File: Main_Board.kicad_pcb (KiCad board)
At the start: 2 copper layers, 90 x 90 mm, 61 parts, among them J1 DAC_12-bits, J2 Measurement_Header, Q1 Q_PNP_BCE, Q2 Q_NPN_BCE, U1 AD667, U2 LF356

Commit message: Stuff
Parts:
- added U3: AD558JN, Package_DIP:DIP-16_W7.62mm_Socket, F.Cu at (81.0, 85.0)
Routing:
- net /Vin: track 173.3 -> 148.1 mm
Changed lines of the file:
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@@
     (thickness 1.6)
     (drawings 11)
-    (tracks 396)
+    (tracks 398)
     (zones 0)
-    (modules 61)
-    (nets 57)
+    (modules 62)
+    (nets 73)
   )
   (page A4)
   (layers
     (0 F.Cu signal)
-    (31 B.Cu signal hide)
+    (31 B.Cu signal)
     (32 B.Adhes user)
     (33 F.Adhes user)
@@
   (net 55 "Net-(+15V1-Pad3)")
   (net 56 "Net-(+15V1-Pad2)")
+  (net 57 "Net-(U3-Pad16)")
+  (net 58 "Net-(U3-Pad8)")
+  (net 59 "Net-(U3-Pad15)")
+  (net 60 "Net-(U3-Pad7)")
+  (net 61 "Net-(U3-Pad14)")
+  (net 62 "Net-(U3-Pad6)")
+  (net 63 "Net-(U3-Pad13)")
+  (net 64 "Net-(U3-Pad5)")
+  (net 65 "Net-(U3-Pad12)")
+  (net 66 "Net-(U3-Pad4)")
+  (net 67 "Net-(U3-Pad11)")
+  (net 68 "Net-(U3-Pad3)")
+  (net 69 "Net-(U3-Pad10)")
+  (net 70 "Net-(U3-Pad2)")
+  (net 71 "Net-(U3-Pad9)")
+  (net 72 "Net-(U3-Pad1)")
   (net_class Default "This is the default net class."
     (clearance 0.2)
@@
     (add_net "Net-(U2-Pad5)")
     (add_net "Net-(U2-Pad8)")
+    (add_net "Net-(U3-Pad1)")
+    (add_net "Net-(U3-Pad10)")
+    (add_net "Net-(U3-Pad11)")
+    (add_net "Net-(U3-Pad12)")
+    (add_net "Net-(U3-Pad13)")
+    (add_net "Net-(U3-Pad14)")
+    (add_net "Net-(U3-Pad15)")
+    (add_net "Net-(U3-Pad16)")
+    (add_net "Net-(U3-Pad2)")
+    (add_net "Net-(U3-Pad3)")
+    (add_net "Net-(U3-Pad4)")
+    (add_net "Net-(U3-Pad5)")
+    (add_net "Net-(U3-Pad6)")
+    (add_net "Net-(U3-Pad7)")
+    (add_net "Net-(U3-Pad8)")
+    (add_net "Net-(U3-Pad9)")
+  )
+  (module Package_DIP:DIP-16_W7.62mm_Socket (layer F.Cu)
+    (at 81 85)
+    (descr "16-lead though-hole mounted DIP package, row spacing 7.62 mm (300 mils), Socket")
+    (tags "THT DIP DIL PDIP 2.54mm 7.62mm 300mil Socket")
+    (fp_text reference U3 (at 3.81 -2.33) (layer F.SilkS)
+      (effects (font (size 1 1) (thickness 0.15)))
+    )
+    (fp_text value AD558JN (at 3.81 20.11) (layer F.Fab)
+      (effects (font (size 1 1) (thickness 0.15)))
+    )
+    (fp_text user %R (at 3.81 8.89) (layer F.Fab)
+      (effects (font (size 1 1) (thickness 0.15)))
+    )
+    (fp_line (start 9.15 -1.6) (end -1.55 -1.6) (layer F.CrtYd) (width 0.05))
+    (fp_line (start 9.15 19.4) (end 9.15 -1.6) (layer F.CrtYd) (width 0.05))
+    (fp_line (start -1.55 19.4) (end 9.15 19.4) (layer F.CrtYd) (width 0.05))
+    (fp_line (start -1.55 -1.6) (end -1.55 19.4) (layer F.CrtYd) (width 0.05))
+    (fp_line (start 8.95 -1.39) (end -1.33 -1.39) (layer F.SilkS) (width 0.12))
+    (fp_line (start 8.95 19.17) (end 8.95 -1.39) (layer F.SilkS) (width 0.12))
+    (fp_line (start -1.33 19.17) (end 8.95 19.17) (layer F.SilkS) (width 0.12))
+    (fp_line (start -1.33 -1.39) (end -1.33 19.17) (layer F.SilkS) (width 0.12))
+    (fp_line (start 6.46 -1.33) (end 4.81 -1.33) (layer F.SilkS) (width 0.12))
+    (fp_line (start 6.46 19.11) (end 6.46 -1.33) (layer F.SilkS) (width 0.12))
+    (fp_line (start 1.16 19.11) (end 6.46 19.11) (layer F.SilkS) (width 0.12))
+    (fp_line (start 1.16 -1.33) (end 1.16 19.11) (layer F.SilkS) (width 0.12))
+    (fp_line (start 2.81 -1.33) (end 1.16 -1.33) (layer F.SilkS) (width 0.12))
+    (fp_line (start 8.89 -1.33) (end -1.27 -1.33) (layer F.Fab) (width 0.1))
+    (fp_line (start 8.89 19.11) (end 8.89 -1.33) (layer F.Fab) (width 0.1))
+    (fp_line (start -1.27 19.11) (end 8.89 19.11) (layer F.Fab) (width 0.1))
+    (fp_line (start -1.27 -1.33) (end -1.27 19.11) (layer F.Fab) (width 0.1))
+    (fp_line (start 0.635 -0.27) (end 1.635 -1.27) (layer F.Fab) (width 0.1))
+    (fp_line (start 0.635 19.05) (end 0.635 -0.27) (layer F.Fab) (width 0.1))
+    (fp_line (start 6.985 19.05) (end 0.635 19.05) (layer F.Fab) (width 0.1))
+    (fp_line (start 6.985 -1.27) (end 6.985 19.05) (layer F.Fab) (width 0.1))
+    (fp_line (start 1.635 -1.27) (end 6.985 -1.27) (layer F.Fab) (width 0.1))
+    (fp_arc (start 3.81 -1.33) (end 2.81 -1.33) (angle -180) (layer F.SilkS) (width 0.12))
+    (pad 16 thru_hole oval (at 7.62 0) (size 1.6 1.6) (drill 0.8) (layers *.Cu *.Mask)
+      (net 57 "Net-(U3-Pad16)"))
+    (pad 8 thru_hole oval (at 0 17.78) (size 1.6 1.6) (drill 0.8) (layers *.Cu *.Mask)
+      (net 58 "Net-(U3-Pad8)"))
+    (pad 15 thru_hole oval (at 7.62 2.54) (size 1.6 1.6) (drill 0.8) (layers *.Cu *.Mask)
+      (net 59 "Net-(U3-Pad15)"))
+    (pad 7 thru_hole oval (at 0 15.24) (size 1.6 1.6) (drill 0.8) (layers *.Cu *.Mask)
+      (net 60 "Net-(U3-Pad7)"))
+    (pad 14 thru_hole oval (at 7.62 5.08) (size 1.6 1.6) (drill 0.8) (layers *.Cu *.Mask)
+      (net 61 "Net-(U3-Pad14)"))
+    (pad 6 thru_hole oval (at 0 12.7) (size 1.6 1.6) (drill 0.8) (layers *.Cu *.Mask)
+      (net 62 "Net-(U3-Pad6)"))
+    (pad 13 thru_hole oval (at 7.62 7.62) (size 1.6 1.6) (drill 0.8) (layers *.Cu *.Mask)
+      (net 63 "Net-(U3-Pad13)"))
+    (pad 5 thru_hole oval (at 0 10.16) (size 1.6 1.6) (drill 0.8) (layers *.Cu *.Mask)
+      (net 64 "Net-(U3-Pad5)"))
+    (pad 12 thru_hole oval (at 7.62 10.16) (size 1.6 1.6) (drill 0.8) (layers *.Cu *.Mask)
+      (net 65 "Net-(U3-Pad12)"))
+    (pad 4 thru_hole oval (at 0 7.62) (size 1.6 1.6) (drill 0.8) (layers *.Cu *.Mask)
+      (net 66 "Net-(U3-Pad4)"))
+    (pad 11 thru_hole oval (at 7.62 12.7) (size 1.6 1.6) (drill 0.8) (layers *.Cu *.Mask)
+      (net 67 "Net-(U3-Pad11)"))
+    (pad 3 thru_hole oval (at 0 5.08) (size 1.6 1.6) (drill 0.8) (layers *.Cu *.Mask)
+      (net 68 "Net-(U3-Pad3)"))
+    (pad 10 thru_hole oval (at 7.62 15.24) (size 1.6 1.6) (drill 0.8) (layers *.Cu *.Mask)
+      (net 69 "Net-(U3-Pad10)"))
+    (pad 2 thru_hole oval (at 0 2.54) (size 1.6 1.6) (drill 0.8) (layers *.Cu *.Mask)
+      (net 70 "Net-(U3-Pad2)"))
+    (pad 9 thru_hole oval (at 7.62 17.78) (size 1.6 1.6) (drill 0.8) (layers *.Cu *.Mask)
+      (net 71 "Net-(U3-Pad9)"))
+    (pad 1 thru_hole rect (at 0 0) (size 1.6 1.6) (drill 0.8) (layers *.Cu *.Mask)
+      (net 72 "Net-(U3-Pad1)"))
+    (model ${KISYS3DMOD}/Package_DIP.3dshapes/DIP-16_W7.62mm_Socket.wrl
+      (at (xyz 0 0 0))
+      (scale (xyz 1 1 1))
+      (rotate (xyz 0 0 0))
+    )
   )
   (module Package_TO_SOT_THT:TO-100-10 (layer F.Cu)
@@
   (segment (start 50.221578 85.222915) (end 51.28233 86.283667) (width 0.25) (layer B.Cu) (net 6))
   (segment (start 49.82233 85.222915) (end 50.221578 85.222915) (width 0.25) (layer B.Cu) (net 6))
-  (segment (start 76.3 81.8) (end 88.2 93.7) (width 0.25) (layer B.Cu) (net 6))
-  (segment (start 88.2 130.7) (end 78 140.9) (width 0.25) (layer B.Cu) (net 6))
-  (segment (start 88.2 93.7) (end 88.2 130.7) (width 0.25) (layer B.Cu) (net 6))
-  (segment (start 50.422329 83.877671) (end 52.5 81.8) (width 0.25) (layer B.Cu) (net 6))
-  (segment (start 50.422329 84.622916) (end 50.422329 83.877671) (width 0.25) (layer B.Cu) (net 6))
-  (segment (start 49.82233 85.222915) (end 50.422329 84.622916) (width 0.25) (layer B.Cu) (net 6))
-  (segment (start 52.5 81.8) (end 76.3 81.8) (width 0.25) (layer B.Cu) (net 6))
-  (segment (start 52.5 81.8) (end 31.6 81.8) (width 0.25) (layer B.Cu) (net 6))
-  (segment (start 30.711917 81.8) (end 31.6 81.8) (width 0.25) (layer B.Cu) (net 6))
-  (segment (start 28.21373 84.298187) (end 30.711917 81.8) (width 0.25) (layer B.Cu) (net 6))
-  (segment (start 28.21373 85.146715) (end 28.21373 84.298187) (width 0.25) (layer B.Cu) (net 6))
   (segment (start 30.522258 86.207467) (end 32.9 88.585209) (width 0.25) (layer B.Cu) (net 6))
   (segment (start 29.67373 86.207467) (end 30.522258 86.207467) (width 0.25) (layer B.Cu) (net 6))
@@
   (segment (start 54.365997 83.2) (end 51.28233 86.283667) (width 0.25) (layer F.Cu) (net 6))
   (segment (start 56.5 83.2) (end 54.365997 83.2) (width 0.25) (layer F.Cu) (net 6))
+  (segment (start 78 140.9) (end 80.1 140.9) (width 0.25) (layer B.Cu) (net 6))
+  (segment (start 80.1 140.9) (end 82 139) (width 0.25) (layer B.Cu) (net 6))
+  (segment (start 82 139) (end 82 113) (width 0.25) (layer B.Cu) (net 6))
+  (segment (start 82 113) (end 72 103) (width 0.25) (layer B.Cu) (net 6))
+  (segment (start 72 103) (end 72 101) (width 0.25) (layer B.Cu) (net 6))
+  (segment (start 72 101) (end 61 90) (width 0.25) (layer B.Cu) (net 6))
+  (segment (start 61 90) (end 57 90) (width 0.25) (layer B.Cu) (net 6))
+  (segment (start 53.283667 86.283667) (end 51.28233 86.283667) (width 0.25) (layer B.Cu) (net 6))
+  (segment (start 57 90) (end 53.283667 86.283667) (width 0.25) (layer B.Cu) (net 6))
+  (segment (start 28.813729 84.546716) (end 28.21373 85.146715) (width 0.25) (layer B.Cu) (net 6))
+  (segment (start 30.760445 82.6) (end 28.813729 84.546716) (width 0.25) (layer B.Cu) (net 6))
+  (segment (start 47.199415 82.6) (end 30.760445 82.6) (width 0.25) (layer B.Cu) (net 6))
+  (segment (start 49.82233 85.222915) (end 47.199415 82.6) (width 0.25) (layer B.Cu) (net 6))
   (segment (start 31 133.15) (end 31 132) (width 0.25) (layer F.Cu) (net 7))
   (segment (start 31 135.1) (end 31 133.15) (width 0.25) (layer F.Cu) (net 7))
@@
     (connect_pads (clearance 0.508))
     (min_thickness 0.254)
-    (fill yes (arc_segments 32) (thermal_gap 0.508) (thermal_bridge_width 0.508))
+    (fill (arc_segments 32) (thermal_gap 0.508) (thermal_bridge_width 0.508))
     (polygon
       (pts

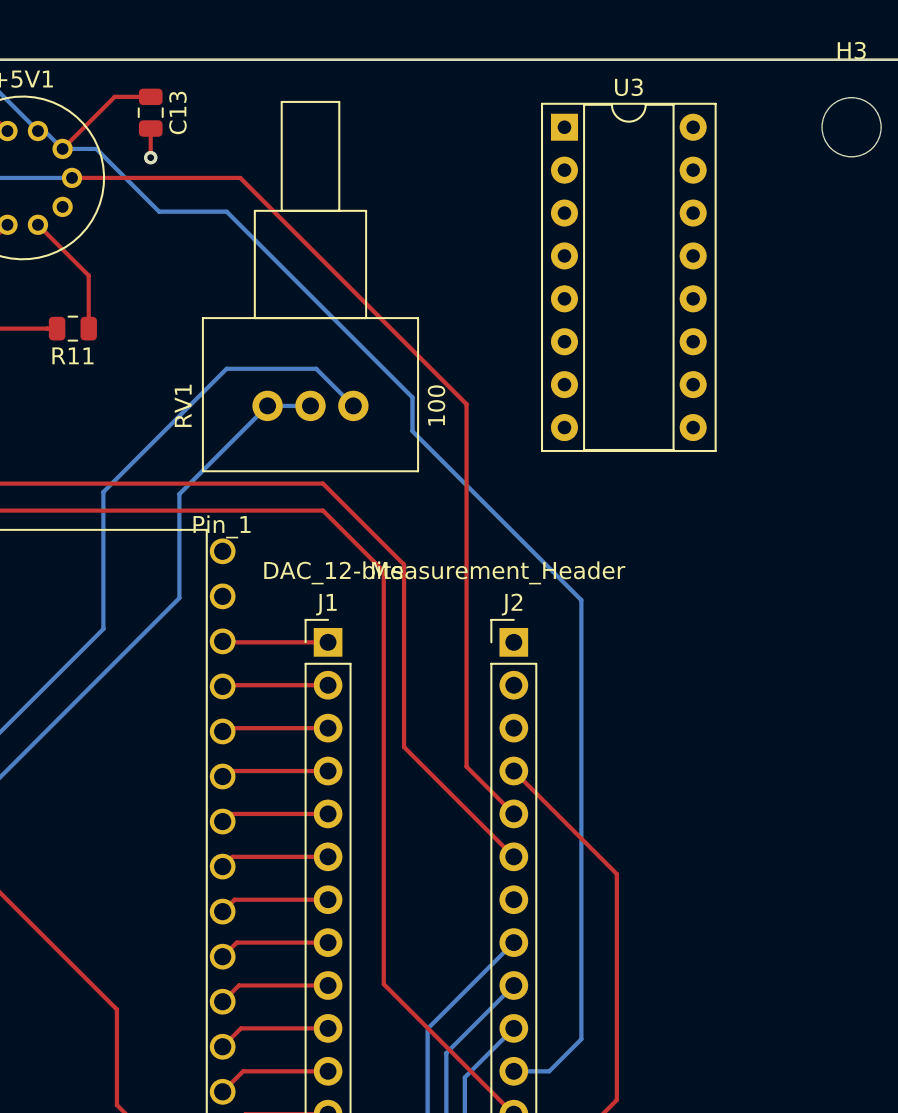
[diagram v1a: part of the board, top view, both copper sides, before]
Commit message: Defined and added 8-bit DAC for CEM transistor base voltage control to schematic and  layout. Still need to do the routing, waiting on clarification of analog output voltage range of 0-2.56V or 0-10V from Riya as this will effect 8-bit DAC pin wiring.
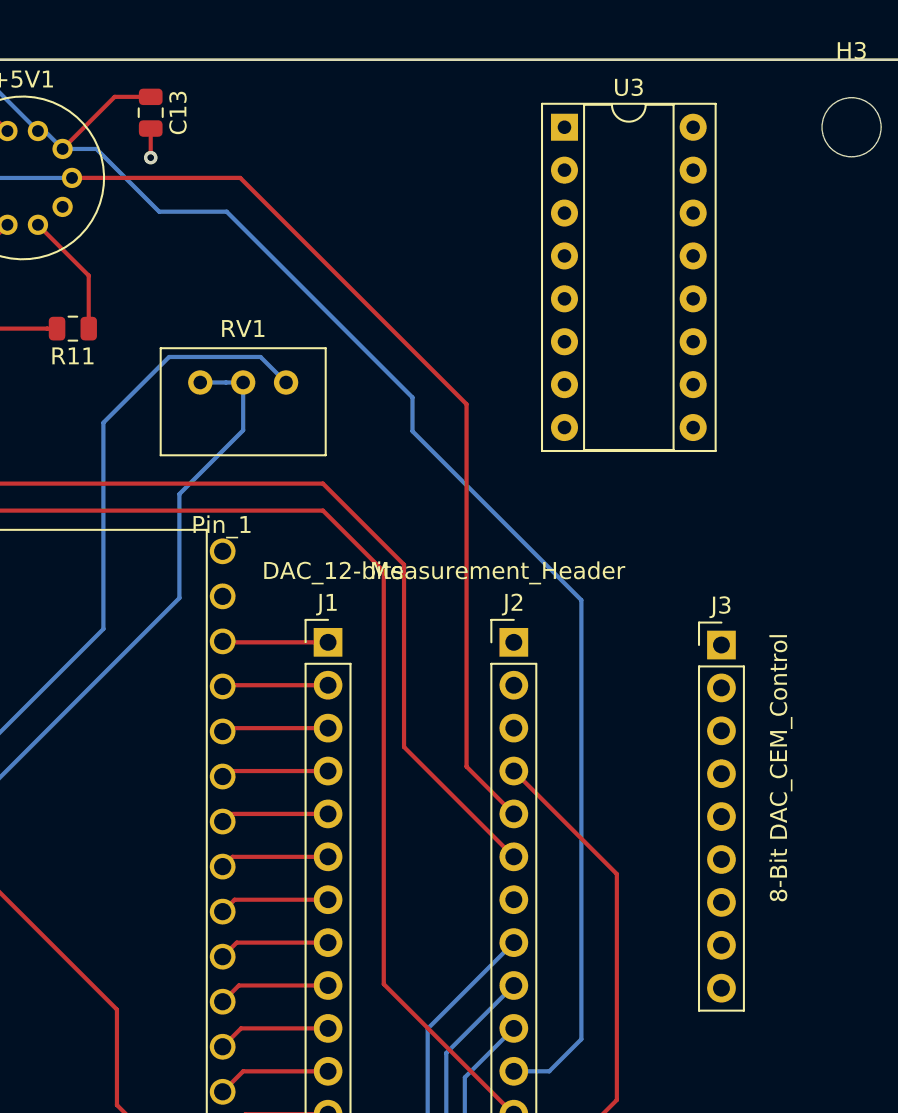
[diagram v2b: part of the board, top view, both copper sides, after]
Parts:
- added J3: 8-Bit DAC_CEM_Control, Connector_PinHeader_2.54mm:PinHeader_1x09_P2.54mm_Vertical, F.Cu at (90.3, 115.7)
- RV1: footprint Potentiometer_THT:Potentiometer_Vishay_148-149_Single_Horizontal -> Potentiometer_THT:Potentiometer_Bourns_3299W_Vertical
- moved RV1 4.22 mm to (64.5, 100.1), turned to 0 degrees
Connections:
- U3 pad 1: Net-(U3-Pad1) -> /MSP430_P2.4_Bit0
- U3 pad 10: Net-(U3-Pad10) -> GND
- U3 pad 11: Net-(U3-Pad11) -> /+15V
- U3 pad 12: Net-(U3-Pad12) -> GND
- U3 pad 13: Net-(U3-Pad13) -> GND
- U3 pad 16: Net-(U3-Pad16) -> /CEM_Trans_Base_Vol
- U3 pad 2: Net-(U3-Pad2) -> /MSP430_P2.5_Bit1
- U3 pad 3: Net-(U3-Pad3) -> /MSP430_P2.6_Bit2
- U3 pad 4: Net-(U3-Pad4) -> /MSP430_P2.7_Bit3
- U3 pad 5: Net-(U3-Pad5) -> /MSP430_P3.0_Bit4
- U3 pad 6: Net-(U3-Pad6) -> /MSP430_P3.1_Bit5
- U3 pad 7: Net-(U3-Pad7) -> /MSP430_P3.2_Bit6
- U3 pad 8: Net-(U3-Pad8) -> /MSP430_P3.3_Bit7
- U3 pad 9: Net-(U3-Pad9) -> GND
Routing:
- net Net-(RV1-Pad1): track 39.2 -> 37.6 mm
- net Net-(RV1-Pad2): track 34.8 -> 35.6 mm

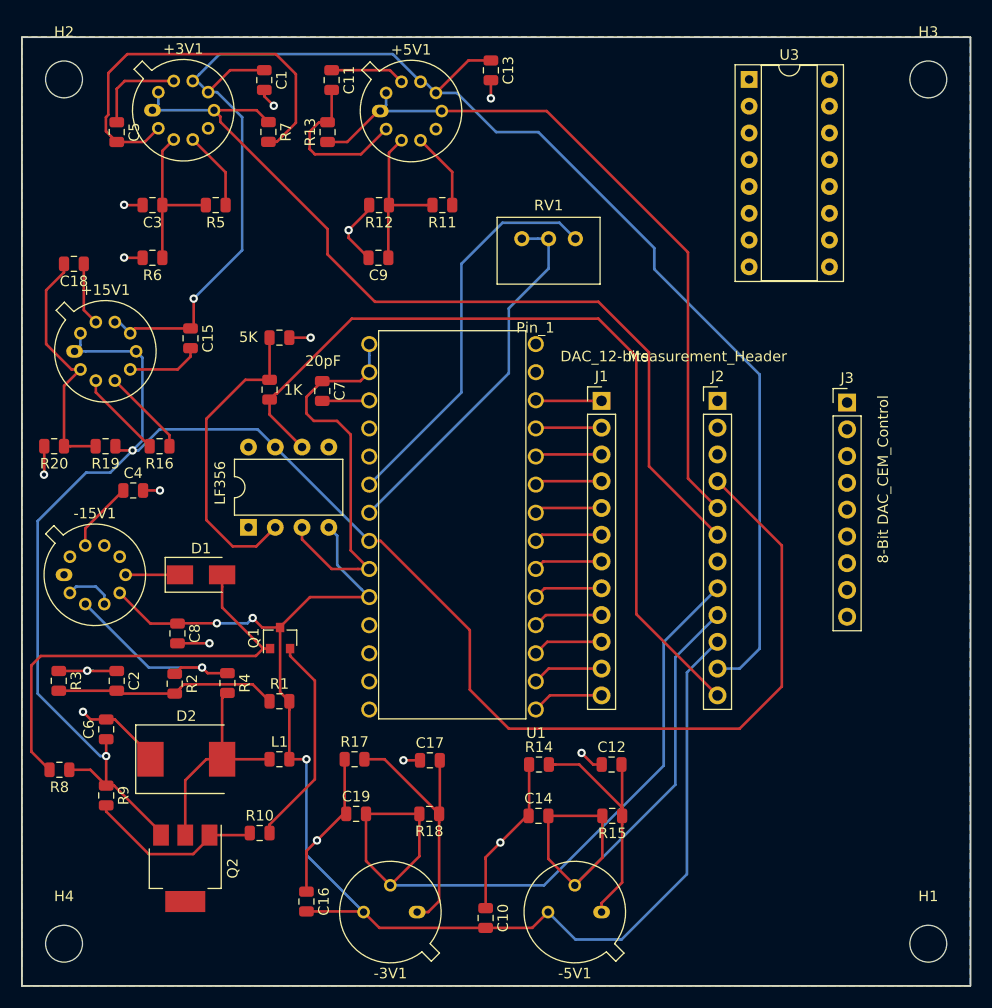
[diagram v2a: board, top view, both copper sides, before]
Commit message: Finished schematic and layout of 8-bit DAC for CEM transistor control. Adding GND plane to bottom copper.
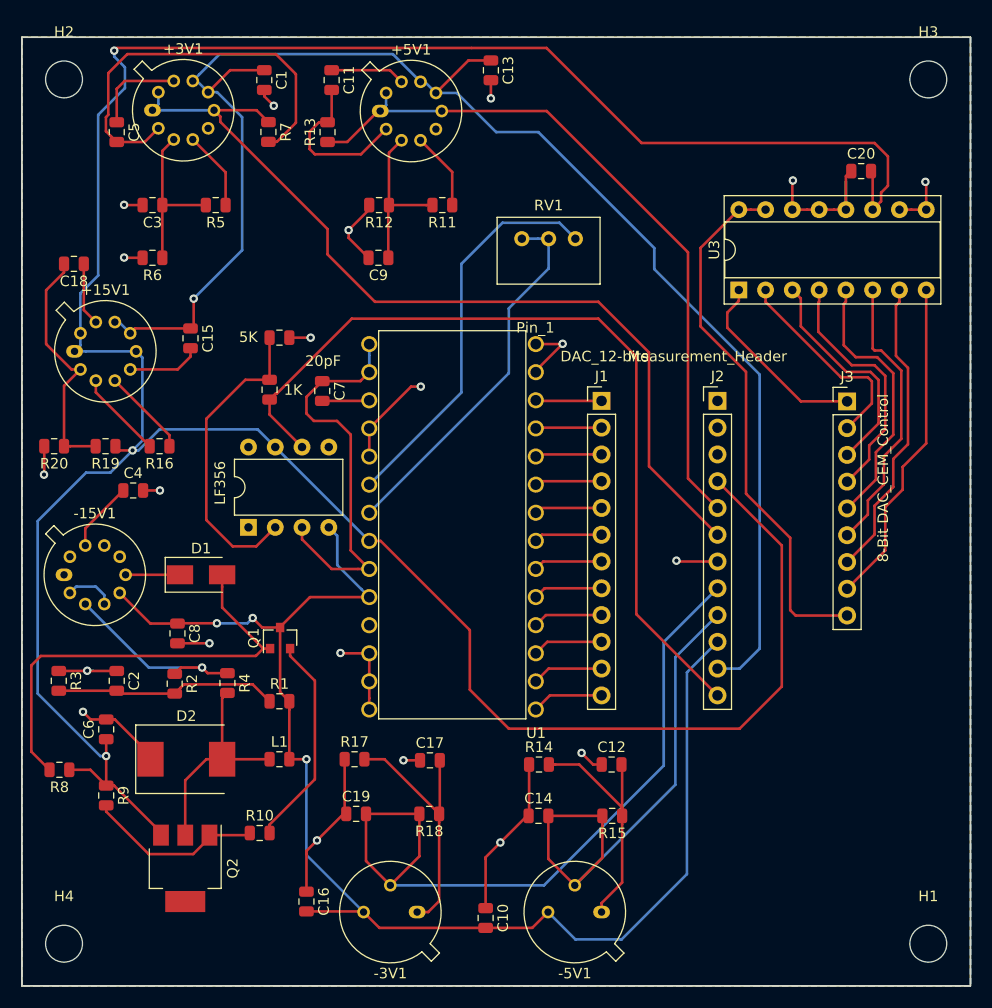
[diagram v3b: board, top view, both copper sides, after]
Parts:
- added C20: 0.1u, Capacitor_SMD:C_0805_2012Metric, F.Cu at (91.6, 93.7)
- moved U3 20.0 mm to (80.0, 105.0), turned to 90 degrees
- moved J3 0.11 mm to (90.3, 115.5)
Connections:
- U3 pad 14: Net-(U3-Pad14) -> GND
- U3 pad 15: Net-(U3-Pad15) -> /CEM_Trans_Base_Vol
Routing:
- net /+15V: track 173.7 -> 289.9 mm, vias 2 -> 3
- net /CEM_Trans_Base_Vol: track 0.00 -> 51.2 mm
- net GND: track 78.4 -> 125.6 mm, vias 15 -> 21
- net /MSP430_P3.3_Bit7: track 0.00 -> 31.5 mm
- net /MSP430_P3.2_Bit6: track 0.00 -> 28.8 mm
- net /MSP430_P3.1_Bit5: track 0.00 -> 26.9 mm
- net /MSP430_P3.0_Bit4: track 0.00 -> 25.8 mm
- net /MSP430_P2.7_Bit3: track 0.00 -> 23.6 mm
- net /MSP430_P2.6_Bit2: track 0.00 -> 21.6 mm
- net /MSP430_P2.5_Bit1: track 0.00 -> 19.8 mm
- net /MSP430_P2.4_Bit0: track 0.00 -> 18.3 mm
